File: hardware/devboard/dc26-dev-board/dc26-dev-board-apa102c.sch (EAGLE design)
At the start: 84 parts, among them CN1 JST, IC1 STM32F411RET6, M10 STM32-Breakout-2, P1 SSSS811101, U1 ESP-WROOM-32, Y1 ABL-8.000MHZ-B2

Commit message: power run not but not gpio
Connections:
- net VCC4: now also U$7.VCC
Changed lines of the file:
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@@
 <?xml version="1.0" encoding="utf-8"?>
 <!DOCTYPE eagle SYSTEM "eagle.dtd">
-<eagle version="8.6.1">
+<eagle version="8.6.3">
 <drawing>
 <settings>
@@
 <wire x1="12.7" y1="-20.32" x2="15.24" y2="-20.32" width="0.1524" layer="91"/>
 <pinref part="C21" gate="G$1" pin="1"/>
-</segment>
-</net>
+<pinref part="U$7" gate="G$1" pin="VCC"/>
+</segment>
+</net>

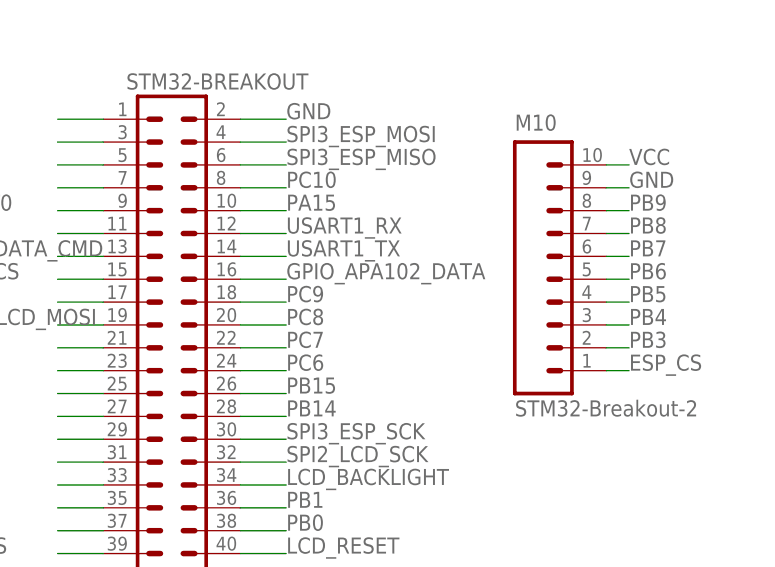
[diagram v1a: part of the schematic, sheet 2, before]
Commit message: ran power to apa102
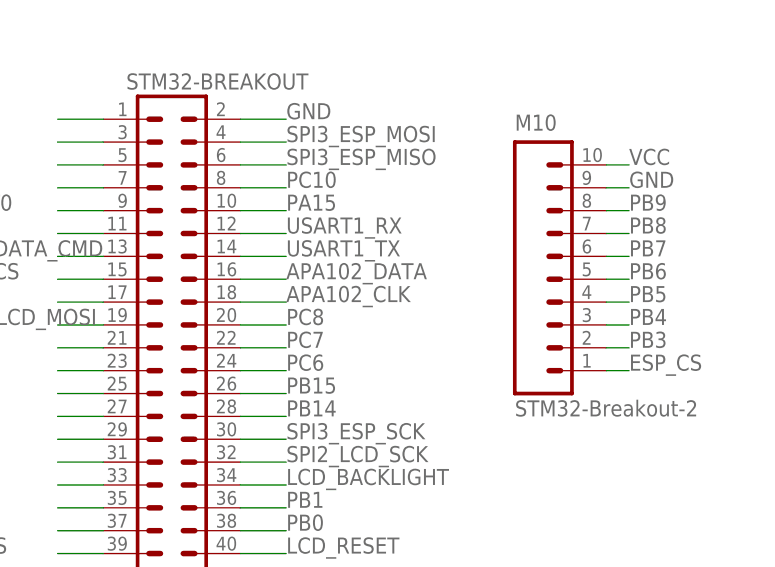
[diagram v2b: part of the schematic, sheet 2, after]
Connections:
- removed net GPIO_APA102_DATA: STM32-BREAKOUT.16
- removed net PC9: STM32-BREAKOUT.18
- removed net VCC10: C27.1
- removed net VCC11: C28.1
- removed net VCC12: C29.1
- removed net VCC13: C30.1
- removed net VCC14: C32.1
- removed net VCC15: C33.1
- removed net VCC16: C34.1
- removed net VCC2: C14.1
- removed net VCC3: C20.1
- removed net VCC4: C21.1, U$7.VCC
- removed net VCC5: C22.1
- removed net VCC6: C23.1
- removed net VCC7: C24.1
- removed net VCC8: C25.1
- removed net VCC9: C26.1
- net APA102_CLK: now also STM32-BREAKOUT.18
- net APA102_DATA: now also STM32-BREAKOUT.16, U$8.DI
- net VCC1: no longer C31.1
- net VIN: now also C14.1, C20.1, C21.1, C22.1, C23.1, C24.1, C25.1, C26.1, C27.1, C28.1, C29.1, C30.1, C31.1, C32.1, C33.1, C34.1, U$10.VCC, U$11.VCC, U$12.VCC, U$13.VCC, U$14.VCC, U$15.VCC, U$16.VCC, U$17.VCC, U$18.VCC, U$19.VCC, U$20.VCC, U$5.VCC, U$6.VCC, U$7.VCC, U$8.VCC, U$9.VCC
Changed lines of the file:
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@@
-</segment>
-</net>
-<net name="GPIO_APA102_DATA" class="0">
-<segment>
-<pinref part="STM32-BREAKOUT" gate="G$1" pin="16"/>
-<wire x1="193.04" y1="53.34" x2="198.12" y2="53.34" width="0.1524" layer="91"/>
-<label x="198.12" y="53.34" size="1.778" layer="95"/>
 </segment>
 </net>
@@
 </segment>
 </net>
-<net name="PC9" class="0">
-<segment>
-<pinref part="STM32-BREAKOUT" gate="G$1" pin="18"/>
-<wire x1="193.04" y1="50.8" x2="198.12" y2="50.8" width="0.1524" layer="91"/>
-<label x="198.12" y="50.8" size="1.778" layer="95"/>
-</segment>
-</net>
 <net name="PC8" class="0">
 <segment>
@@
 <label x="132.08" y="45.72" size="1.778" layer="95"/>
 </segment>
+<segment>
+<pinref part="STM32-BREAKOUT" gate="G$1" pin="18"/>
+<wire x1="193.04" y1="50.8" x2="198.12" y2="50.8" width="0.1524" layer="91"/>
+<label x="198.12" y="50.8" size="1.778" layer="95"/>
+</segment>
 </net>
 <net name="APA102_DATA" class="0">
@@
 <wire x1="127" y1="48.26" x2="129.54" y2="48.26" width="0.1524" layer="91"/>
 <label x="132.08" y="48.26" size="1.778" layer="95"/>
+</segment>
+<segment>
+<pinref part="STM32-BREAKOUT" gate="G$1" pin="16"/>
+<wire x1="193.04" y1="53.34" x2="198.12" y2="53.34" width="0.1524" layer="91"/>
+<label x="198.12" y="53.34" size="1.778" layer="95"/>
 </segment>
 </net>
@@
 </segment>
 </net>
-<net name="VCC1" class="0">
-<segment>
-<wire x1="12.7" y1="101.6" x2="15.24" y2="101.6" width="0.1524" layer="91"/>
-<pinref part="C31" gate="G$1" pin="1"/>
-</segment>
-</net>
 <net name="APA102_CLK" class="0">
 <segment>
@@
 <net name="APA102_DATA" class="0">
 <segment>
-<wire x1="7.62" y1="129.54" x2="7.62" y2="111.76" width="0.1524" layer="91"/>
+<wire x1="7.62" y1="129.54" x2="7.62" y2="114.3" width="0.1524" layer="91"/>
 <label x="10.16" y="111.76" size="1.778" layer="95" rot="R90"/>
-</segment>
-</net>
-<net name="VCC2" class="0">
-<segment>
-<wire x1="12.7" y1="60.96" x2="15.24" y2="60.96" width="0.1524" layer="91"/>
-<pinref part="C14" gate="G$1" pin="1"/>
-</segment>
-</net>
-<net name="VCC3" class="0">
-<segment>
-<wire x1="12.7" y1="20.32" x2="15.24" y2="20.32" width="0.1524" layer="91"/>
-<pinref part="C20" gate="G$1" pin="1"/>
-</segment>
-</net>
-<net name="VCC4" class="0">
-<segment>
-<wire x1="12.7" y1="-20.32" x2="15.24" y2="-20.32" width="0.1524" layer="91"/>
-<pinref part="C21" gate="G$1" pin="1"/>
-<pinref part="U$7" gate="G$1" pin="VCC"/>
-</segment>
-</net>
-<net name="VCC5" class="0">
-<segment>
-<wire x1="45.72" y1="-5.08" x2="43.18" y2="-5.08" width="0.1524" layer="91"/>
-<pinref part="C22" gate="G$1" pin="1"/>
-</segment>
-</net>
-<net name="VCC6" class="0">
-<segment>
-<wire x1="45.72" y1="35.56" x2="43.18" y2="35.56" width="0.1524" layer="91"/>
-<pinref part="C23" gate="G$1" pin="1"/>
-</segment>
-</net>
-<net name="VCC7" class="0">
-<segment>
-<wire x1="45.72" y1="76.2" x2="43.18" y2="76.2" width="0.1524" layer="91"/>
-<pinref part="C24" gate="G$1" pin="1"/>
-</segment>
-</net>
-<net name="VCC8" class="0">
-<segment>
-<wire x1="45.72" y1="116.84" x2="43.18" y2="116.84" width="0.1524" layer="91"/>
-<pinref part="C25" gate="G$1" pin="1"/>
-</segment>
-</net>
-<net name="VCC9" class="0">
-<segment>
-<wire x1="96.52" y1="101.6" x2="99.06" y2="101.6" width="0.1524" layer="91"/>
-<pinref part="C26" gate="G$1" pin="1"/>
-</segment>
-</net>
-<net name="VCC10" class="0">
-<segment>
-<wire x1="96.52" y1="60.96" x2="99.06" y2="60.96" width="0.1524" layer="91"/>
-<pinref part="C27" gate="G$1" pin="1"/>
-</segment>
-</net>
-<net name="VCC11" class="0">
-<segment>
-<wire x1="96.52" y1="20.32" x2="99.06" y2="20.32" width="0.1524" layer="91"/>
-<pinref part="C28" gate="G$1" pin="1"/>
-</segment>
-</net>
-<net name="VCC12" class="0">
-<segment>
-<wire x1="96.52" y1="-20.32" x2="99.06" y2="-20.32" width="0.1524" layer="91"/>
-<pinref part="C29" gate="G$1" pin="1"/>
-</segment>
-</net>
-<net name="VCC13" class="0">
-<segment>
-<wire x1="121.92" y1="-5.08" x2="119.38" y2="-5.08" width="0.1524" layer="91"/>
-<pinref part="C30" gate="G$1" pin="1"/>
-</segment>
-</net>
-<net name="VCC14" class="0">
-<segment>
-<wire x1="121.92" y1="35.56" x2="119.38" y2="35.56" width="0.1524" layer="91"/>
-<pinref part="C32" gate="G$1" pin="1"/>
-</segment>
-</net>
-<net name="VCC15" class="0">
-<segment>
-<wire x1="121.92" y1="76.2" x2="119.38" y2="76.2" width="0.1524" layer="91"/>
-<pinref part="C33" gate="G$1" pin="1"/>
-</segment>
-</net>
-<net name="VCC16" class="0">
-<segment>
-<wire x1="121.92" y1="116.84" x2="119.38" y2="116.84" width="0.1524" layer="91"/>
-<pinref part="C34" gate="G$1" pin="1"/>
+<pinref part="U$8" gate="G$1" pin="DI"/>
 </segment>
 </net>
@@
 <pinref part="U$20" gate="G$1" pin="DI"/>
 <wire x1="127" y1="86.36" x2="127" y2="104.14" width="0.1524" layer="91"/>
+</segment>
+</net>
+<net name="VIN" class="0">
+<segment>
+<wire x1="12.7" y1="101.6" x2="15.24" y2="101.6" width="0.1524" layer="91"/>
+<pinref part="C31" gate="G$1" pin="1"/>
+<pinref part="U$8" gate="G$1" pin="VCC"/>
+</segment>
+<segment>
+<wire x1="12.7" y1="60.96" x2="15.24" y2="60.96" width="0.1524" layer="91"/>
+<pinref part="C14" gate="G$1" pin="1"/>
+<pinref part="U$5" gate="G$1" pin="VCC"/>
+</segment>
+<segment>
+<wire x1="12.7" y1="20.32" x2="15.24" y2="20.32" width="0.1524" layer="91"/>
+<pinref part="C20" gate="G$1" pin="1"/>
+<pinref part="U$6" gate="G$1" pin="VCC"/>
+</segment>
+<segment>
+<wire x1="12.7" y1="-20.32" x2="15.24" y2="-20.32" width="0.1524" layer="91"/>
+<pinref part="C21" gate="G$1" pin="1"/>
+<pinref part="U$7" gate="G$1" pin="VCC"/>
+</segment>
+<segment>
+<wire x1="45.72" y1="-5.08" x2="43.18" y2="-5.08" width="0.1524" layer="91"/>
+<pinref part="C22" gate="G$1" pin="1"/>
+<pinref part="U$9" gate="G$1" pin="VCC"/>
+</segment>
+<segment>
+<wire x1="45.72" y1="35.56" x2="43.18" y2="35.56" width="0.1524" layer="91"/>
+<pinref part="C23" gate="G$1" pin="1"/>
+<pinref part="U$10" gate="G$1" pin="VCC"/>
+</segment>
+<segment>
+<wire x1="45.72" y1="76.2" x2="43.18" y2="76.2" width="0.1524" layer="91"/>
+<pinref part="C24" gate="G$1" pin="1"/>
+<pinref part="U$11" gate="G$1" pin="VCC"/>
+</segment>
+<segment>
+<wire x1="45.72" y1="116.84" x2="43.18" y2="116.84" width="0.1524" layer="91"/>
+<pinref part="C25" gate="G$1" pin="1"/>
+<pinref part="U$12" gate="G$1" pin="VCC"/>
+</segment>
+<segment>
+<wire x1="96.52" y1="101.6" x2="99.06" y2="101.6" width="0.1524" layer="91"/>
+<pinref part="C26" gate="G$1" pin="1"/>
+<pinref part="U$13" gate="G$1" pin="VCC"/>
+</segment>
+<segment>
+<wire x1="96.52" y1="60.96" x2="99.06" y2="60.96" width="0.1524" layer="91"/>
+<pinref part="C27" gate="G$1" pin="1"/>
+<pinref part="U$14" gate="G$1" pin="VCC"/>
+</segment>
+<segment>
+<wire x1="96.52" y1="20.32" x2="99.06" y2="20.32" width="0.1524" layer="91"/>
+<pinref part="C28" gate="G$1" pin="1"/>
+<pinref part="U$15" gate="G$1" pin="VCC"/>
+</segment>
+<segment>
+<wire x1="96.52" y1="-20.32" x2="99.06" y2="-20.32" width="0.1524" layer="91"/>
+<pinref part="C29" gate="G$1" pin="1"/>
+<pinref part="U$16" gate="G$1" pin="VCC"/>
+</segment>
+<segment>
+<wire x1="121.92" y1="-5.08" x2="119.38" y2="-5.08" width="0.1524" layer="91"/>
+<pinref part="C30" gate="G$1" pin="1"/>
+<pinref part="U$17" gate="G$1" pin="VCC"/>
+</segment>
+<segment>
+<wire x1="121.92" y1="35.56" x2="119.38" y2="35.56" width="0.1524" layer="91"/>
+<pinref part="C32" gate="G$1" pin="1"/>
+<pinref part="U$18" gate="G$1" pin="VCC"/>
+</segment>
+<segment>
+<wire x1="121.92" y1="76.2" x2="119.38" y2="76.2" width="0.1524" layer="91"/>
+<pinref part="C33" gate="G$1" pin="1"/>
+<pinref part="U$19" gate="G$1" pin="VCC"/>
+</segment>
+<segment>
+<wire x1="121.92" y1="116.84" x2="119.38" y2="116.84" width="0.1524" layer="91"/>
+<pinref part="C34" gate="G$1" pin="1"/>
+<pinref part="U$20" gate="G$1" pin="VCC"/>
 </segment>
 </net>
@@
 </sheet>
 </sheets>
+<errors>
+</errors>
 </schematic>
 </drawing>
